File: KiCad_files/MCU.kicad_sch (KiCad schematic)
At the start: 12 parts, among them U1 B3U-1000P, U12 ESP32-S3-MINI-1U

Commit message: wippistä
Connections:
- net GNSS_FIX: now also U12.20 (IO16); no longer U12.18 (IO14)
- net GNSS_HW_R: now also U12.22 (IO18); no longer U12.20 (IO16)
- net GNSS_TM: now also U12.21 (IO17); no longer U12.19 (IO15)
- net UART_RX: now also U12.19 (IO15); no longer U12.22 (IO18)
- net UART_TX: now also U12.18 (IO14); no longer U12.21 (IO17)
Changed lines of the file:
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@@
+		)
+	)
+	(hierarchical_label "UART_TX"
+		(shape output)
+		(at 144.78 120.65 180)
+		(effects
+			(font
+				(size 1.27 1.27)
+			)
+			(justify right)
+		)
+	)
+	(hierarchical_label "GNSS_TM"
+		(shape input)
+		(at 144.78 128.27 180)
+		(effects
+			(font
+				(size 1.27 1.27)
+			)
+			(justify right)
 		)
 	)
@@
 		)
 	)
-	(hierarchical_label "GNSS_TM"
+	(hierarchical_label "IO39"
+		(shape bidirectional)
+		(at 194.31 113.03 0)
+		(effects
+			(font
+				(size 1.27 1.27)
+			)
+			(justify left)
+		)
+	)
+	(hierarchical_label "GNSS_HW_R"
+		(shape output)
+		(at 144.78 130.81 180)
+		(effects
+			(font
+				(size 1.27 1.27)
+			)
+			(justify right)
+		)
+	)
+	(hierarchical_label "IO36"
+		(shape bidirectional)
+		(at 194.31 105.41 0)
+		(effects
+			(font
+				(size 1.27 1.27)
+			)
+			(justify left)
+		)
+	)
+	(hierarchical_label "IMU_BOOTN"
+		(shape output)
+		(at 144.78 100.33 180)
+		(effects
+			(font
+				(size 1.27 1.27)
+			)
+			(justify right)
+		)
+	)
+	(hierarchical_label "IO35"
+		(shape bidirectional)
+		(at 194.31 102.87 0)
+		(effects
+			(font
+				(size 1.27 1.27)
+			)
+			(justify left)
+		)
+	)
+	(hierarchical_label "BAT_STAT"
+		(shape input)
+		(at 194.31 130.81 0)
+		(effects
+			(font
+				(size 1.27 1.27)
+			)
+			(justify left)
+		)
+	)
+	(hierarchical_label "IO38"
+		(shape bidirectional)
+		(at 194.31 110.49 0)
+		(effects
+			(font
+				(size 1.27 1.27)
+			)
+			(justify left)
+		)
+	)
+	(hierarchical_label "IO42"
+		(shape bidirectional)
+		(at 194.31 120.65 0)
+		(effects
+			(font
+				(size 1.27 1.27)
+			)
+			(justify left)
+		)
+	)
+	(hierarchical_label "USB_D-"
+		(shape bidirectional)
+		(at 194.31 87.63 0)
+		(effects
+			(font
+				(size 1.27 1.27)
+			)
+			(justify left)
+		)
+	)
+	(hierarchical_label "IO37"
+		(shape bidirectional)
+		(at 194.31 107.95 0)
+		(effects
+			(font
+				(size 1.27 1.27)
+			)
+			(justify left)
+		)
+	)
+	(hierarchical_label "USB_D+"
+		(shape bidirectional)
+		(at 194.31 90.17 0)
+		(effects
+			(font
+				(size 1.27 1.27)
+			)
+			(justify left)
+		)
+	)
+	(hierarchical_label "IO40"
+		(shape bidirectional)
+		(at 194.31 115.57 0)
+		(effects
+			(font
+				(size 1.27 1.27)
+			)
+			(justify left)
+		)
+	)
+	(hierarchical_label "I2C_CLK"
+		(shape output)
+		(at 76.2 118.11 180)
+		(effects
+			(font
+				(size 1.27 1.27)
+			)
+			(justify right)
+		)
+	)
+	(hierarchical_label "IMU_INT"
+		(shape input)
+		(at 144.78 95.25 180)
+		(effects
+			(font
+				(size 1.27 1.27)
+			)
+			(justify right)
+		)
+	)
+	(hierarchical_label "I2C_SDA"
+		(shape bidirectional)
+		(at 76.2 115.57 180)
+		(effects
+			(font
+				(size 1.27 1.27)
+			)
+			(justify right)
+		)
+	)
+	(hierarchical_label "IO41"
+		(shape bidirectional)
+		(at 194.31 118.11 0)
+		(effects
+			(font
+				(size 1.27 1.27)
+			)
+			(justify left)
+		)
+	)
+	(hierarchical_label "IO44"
+		(shape bidirectional)
+		(at 194.31 82.55 0)
+		(effects
+			(font
+				(size 1.27 1.27)
+			)
+			(justify left)
+		)
+	)
+	(hierarchical_label "GNSS_HW_S"
+		(shape output)
+		(at 144.78 118.11 180)
+		(effects
+			(font
+				(size 1.27 1.27)
+			)
+			(justify right)
+		)
+	)
+	(hierarchical_label "UART_RX"
 		(shape input)
 		(at 144.78 123.19 180)
@@
 		)
 	)
-	(hierarchical_label "IO39"
-		(shape bidirectional)
-		(at 194.31 113.03 0)
-		(effects
-			(font
-				(size 1.27 1.27)
-			)
-			(justify left)
-		)
-	)
-	(hierarchical_label "IO36"
-		(shape bidirectional)
-		(at 194.31 105.41 0)
-		(effects
-			(font
-				(size 1.27 1.27)
-			)
-			(justify left)
-		)
-	)
-	(hierarchical_label "IMU_BOOTN"
-		(shape output)
-		(at 144.78 100.33 180)
-		(effects
-			(font
-				(size 1.27 1.27)
-			)
-			(justify right)
-		)
-	)
-	(hierarchical_label "IO35"
-		(shape bidirectional)
-		(at 194.31 102.87 0)
-		(effects
-			(font
-				(size 1.27 1.27)
-			)
-			(justify left)
-		)
-	)
-	(hierarchical_label "BAT_STAT"
-		(shape input)
-		(at 194.31 130.81 0)
-		(effects
-			(font
-				(size 1.27 1.27)
-			)
-			(justify left)
-		)
-	)
-	(hierarchical_label "IO38"
-		(shape bidirectional)
-		(at 194.31 110.49 0)
-		(effects
-			(font
-				(size 1.27 1.27)
-			)
-			(justify left)
-		)
-	)
-	(hierarchical_label "GNSS_HW_R"
-		(shape output)
+	(hierarchical_label "IO43"
+		(shape bidirectional)
+		(at 194.31 80.01 0)
+		(effects
+			(font
+				(size 1.27 1.27)
+			)
+			(justify left)
+		)
+	)
+	(hierarchical_label "IMU_NRST"
+		(shape output)
+		(at 144.78 97.79 180)
+		(effects
+			(font
+				(size 1.27 1.27)
+			)
+			(justify right)
+		)
+	)
+	(hierarchical_label "GNSS_FIX"
+		(shape input)
 		(at 144.78 125.73 180)
 		(effects
 			(font
-				(size 1.27 1.27)
-			)
-			(justify right)
-		)
-	)
-	(hierarchical_label "IO42"
-		(shape bidirectional)
-		(at 194.31 120.65 0)
-		(effects
-			(font
-				(size 1.27 1.27)
-			)
-			(justify left)
-		)
-	)
-	(hierarchical_label "GNSS_FIX"
-		(shape input)
-		(at 144.78 120.65 180)
-		(effects
-			(font
-				(size 1.27 1.27)
-			)
-			(justify right)
-		)
-	)
-	(hierarchical_label "USB_D-"
-		(shape bidirectional)
-		(at 194.31 87.63 0)
-		(effects
-			(font
-				(size 1.27 1.27)
-			)
-			(justify left)
-		)
-	)
-	(hierarchical_label "UART_RX"
-		(shape input)
-		(at 144.78 130.81 180)
-		(effects
-			(font
-				(size 1.27 1.27)
-			)
-			(justify right)
-		)
-	)
-	(hierarchical_label "IO37"
-		(shape bidirectional)
-		(at 194.31 107.95 0)
-		(effects
-			(font
-				(size 1.27 1.27)
-			)
-			(justify left)
-		)
-	)
-	(hierarchical_label "USB_D+"
-		(shape bidirectional)
-		(at 194.31 90.17 0)
-		(effects
-			(font
-				(size 1.27 1.27)
-			)
-			(justify left)
-		)
-	)
-	(hierarchical_label "IO40"
-		(shape bidirectional)
-		(at 194.31 115.57 0)
-		(effects
-			(font
-				(size 1.27 1.27)
-			)
-			(justify left)
-		)
-	)
-	(hierarchical_label "I2C_CLK"
-		(shape output)
-		(at 76.2 118.11 180)
-		(effects
-			(font
-				(size 1.27 1.27)
-			)
-			(justify right)
-		)
-	)
-	(hierarchical_label "IMU_INT"
-		(shape input)
-		(at 144.78 95.25 180)
-		(effects
-			(font
-				(size 1.27 1.27)
-			)
-			(justify right)
-		)
-	)
-	(hierarchical_label "I2C_SDA"
-		(shape bidirectional)
-		(at 76.2 115.57 180)
-		(effects
-			(font
-				(size 1.27 1.27)
-			)
-			(justify right)
-		)
-	)
-	(hierarchical_label "IO41"
-		(shape bidirectional)
-		(at 194.31 118.11 0)
-		(effects
-			(font
-				(size 1.27 1.27)
-			)
-			(justify left)
-		)
-	)
-	(hierarchical_label "IO44"
-		(shape bidirectional)
-		(at 194.31 82.55 0)
-		(effects
-			(font
-				(size 1.27 1.27)
-			)
-			(justify left)
-		)
-	)
-	(hierarchical_label "GNSS_HW_S"
-		(shape output)
-		(at 144.78 118.11 180)
-		(effects
-			(font
-				(size 1.27 1.27)
-			)
-			(justify right)
-		)
-	)
-	(hierarchical_label "IO43"
-		(shape bidirectional)
-		(at 194.31 80.01 0)
-		(effects
-			(font
-				(size 1.27 1.27)
-			)
-			(justify left)
-		)
-	)
-	(hierarchical_label "UART_TX"
-		(shape output)
-		(at 144.78 128.27 180)
-		(effects
-			(font
-				(size 1.27 1.27)
-			)
-			(justify right)
-		)
-	)
-	(hierarchical_label "IMU_NRST"
-		(shape output)
-		(at 144.78 97.79 180)
-		(effects
-			(font

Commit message: wip
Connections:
- net BAROMETER_INT: now also U12.16 (IO12); no longer U12.11 (IO7)
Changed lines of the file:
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@@
-	)
-	(no_connect
-		(at 144.78 115.57)
 	)
 	(no_connect
@@
 	(no_connect
 		(at 194.31 97.79)
+	)
+	(no_connect
+		(at 144.78 102.87)
 	)
 	(wire
@@
 		)
 	)
-	(hierarchical_label "BAROMETER_INT"
-		(shape input)
-		(at 144.78 102.87 180)
-		(effects
-			(font
-				(size 1.27 1.27)
-			)
-			(justify right)
-		)
-	)
 	(hierarchical_label "IO39"
 		(shape bidirectional)
@@
 		(effects
 			(font
+				(size 1.27 1.27)
+			)
+			(justify right)
+		)
+	)
+	(hierarchical_label "BAROMETER_INT"
+		(shape input)
+		(at 144.78 115.57 180)
+		(effects
+			(font

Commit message: liitoksia
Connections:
- net BAROMETER_INT: now also U12.14 (IO10); no longer U12.16 (IO12)
- net BAT_STAT: now also U12.16 (IO12); no longer U12.30 (IO48)
- net I2C_CLK: now also U12.13 (IO9); no longer U12.6 (IO2)
- net I2C_SDA: now also U12.12 (IO8); no longer U12.5 (IO1)
- net IMU_BOOTN: now also U12.11 (IO7); no longer U12.10 (IO6)
- net IMU_INT: now also U12.9 (IO5); no longer U12.8 (IO4)
- net IMU_NRST: now also U12.10 (IO6); no longer U12.9 (IO5)

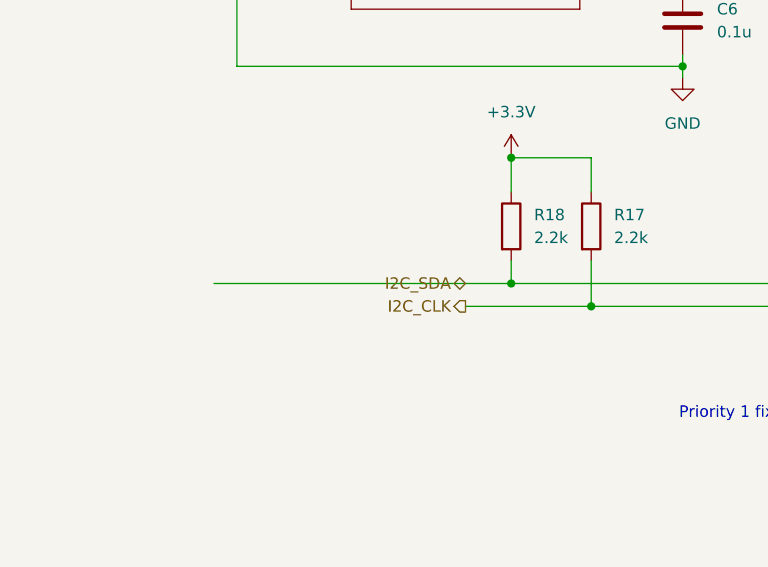
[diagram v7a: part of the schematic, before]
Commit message: copper fillin minimietäisyys laskettu vastaamaan valmistajan speksiä, vioja yms
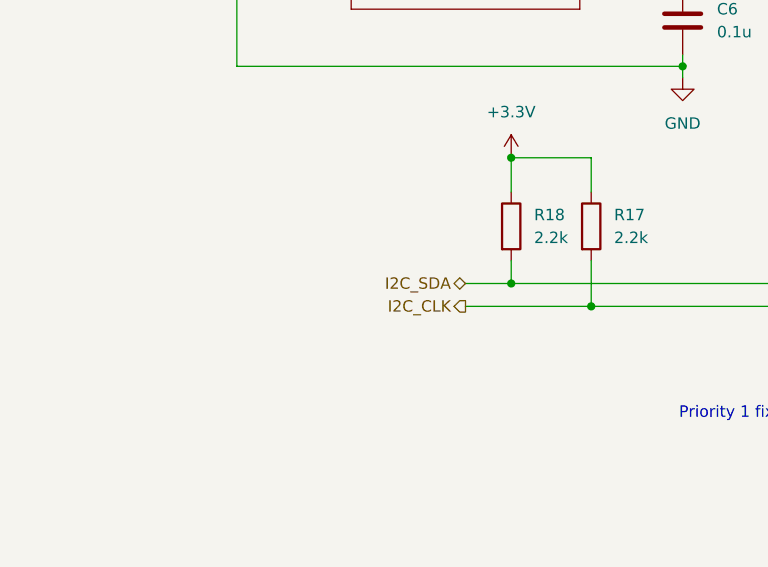
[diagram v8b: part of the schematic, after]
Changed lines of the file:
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@@
 	(wire
 		(pts
-			(xy 48.26 115.57) (xy 81.28 115.57)
+			(xy 76.2 115.57) (xy 81.28 115.57)
 		)
 		(stroke
